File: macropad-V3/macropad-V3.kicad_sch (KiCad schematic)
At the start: 12 parts, among them SW1 SW_Push, U1 ARDUINO_PRO_MICRO

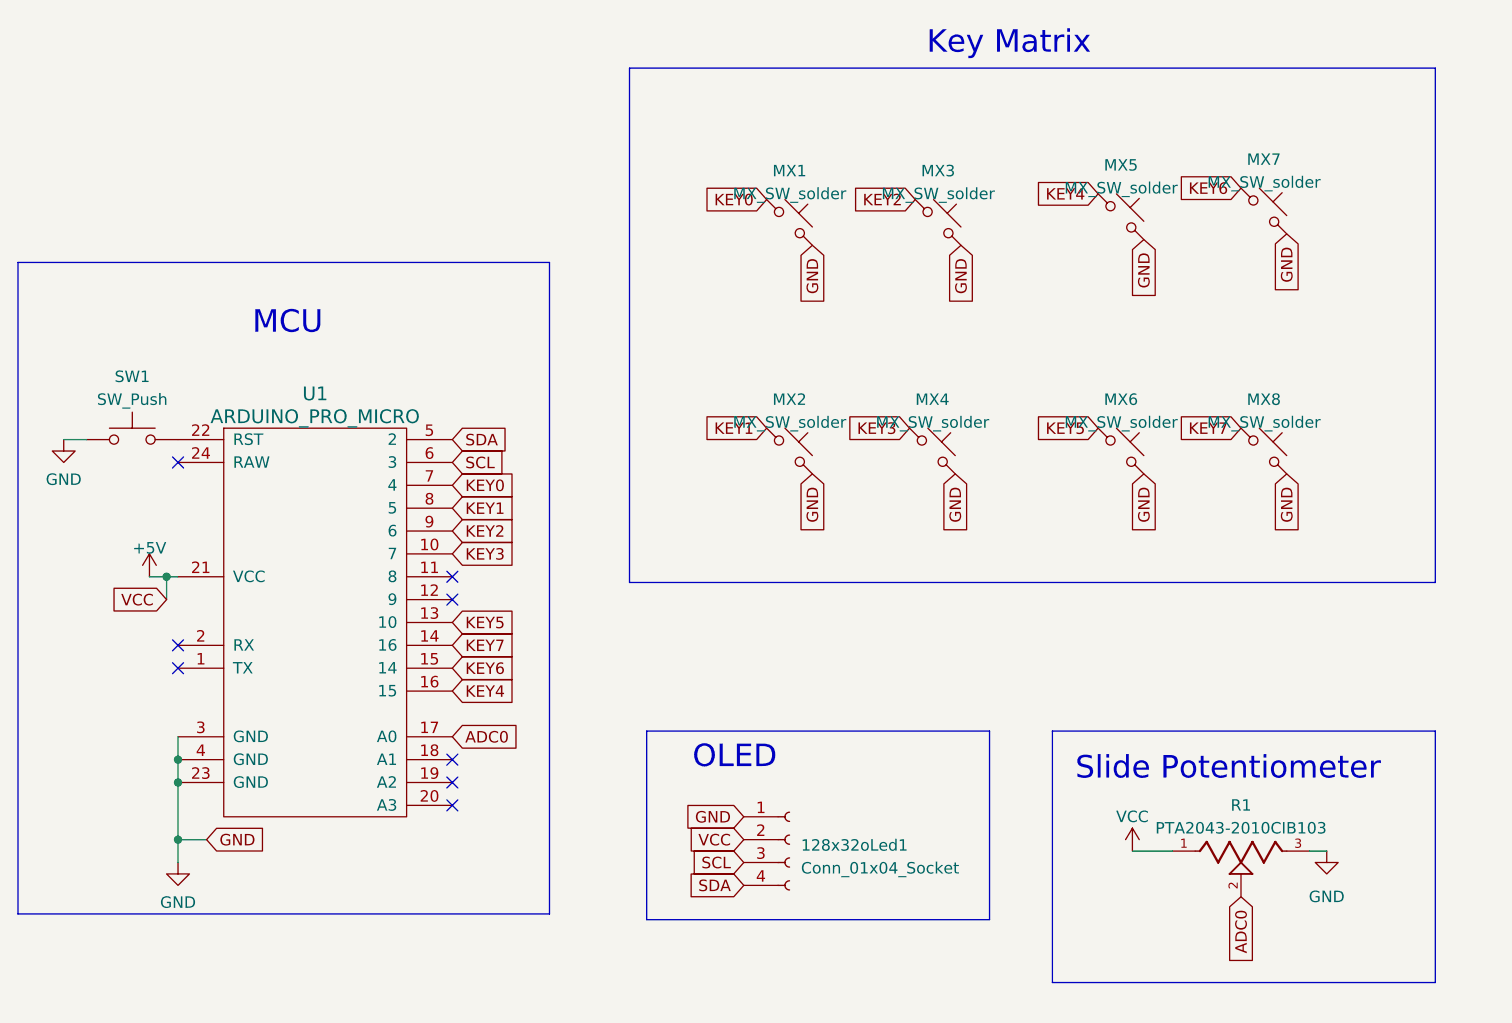
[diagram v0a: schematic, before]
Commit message: finalized schematic
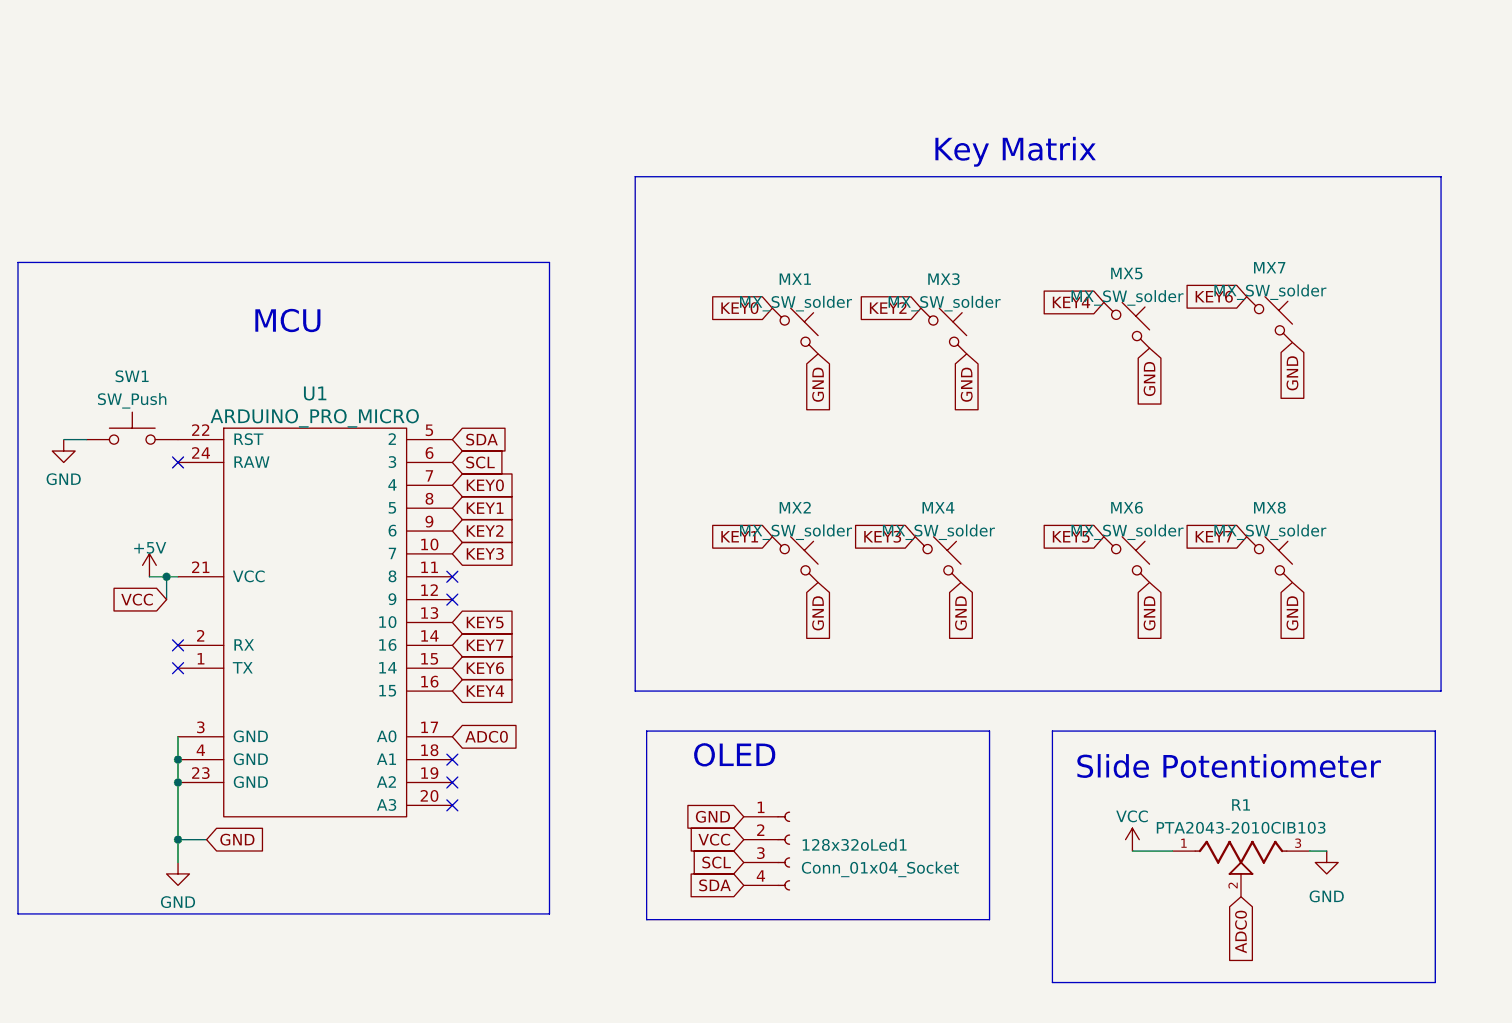
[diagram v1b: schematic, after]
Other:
- moved on the sheet: MX1, MX2, MX3, MX4, MX5, MX6, MX7, MX8

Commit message: added pull up resistors/added ground plane/routed traces
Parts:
- added R2, R3: 4.7k, Resistor_THT:R_Axial_DIN0309_L9.0mm_D3.2mm_P12.70mm_Horizontal, symbol Device:R_Small
- 128x32oLed1: symbol Connector:Conn_01x04_Socket -> Connector_Generic:Conn_01x04
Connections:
- net +5V: now also R2.2, R3.2
- net SCL: now also R2.1
- net SDA: now also R3.1
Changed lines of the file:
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@@
   (junction (at 116.84 128.27) (diameter 0) (color 0 0 0 0)
+  )
+  (junction (at 179.705 139.7) (diameter 0) (color 0 0 0 0)
+  )
+  (junction (at 178.435 137.16) (diameter 0) (color 0 0 0 0)
   )
   (junction (at 116.84 125.73) (diameter 0) (color 0 0 0 0)
@@
     (stroke (width 0) (type default))
   )
+  (wire (pts (xy 178.435 137.16) (xy 178.435 144.78))
+    (stroke (width 0) (type default))
+  )
   (wire (pts (xy 242.57 135.89) (xy 244.475 135.89))
     (stroke (width 0) (type default))
@@
     (stroke (width 0) (type default))
   )
+  (wire (pts (xy 189.23 149.86) (xy 192.405 149.86))
+    (stroke (width 0) (type default))
+  )
+  (wire (pts (xy 174.625 149.86) (xy 178.435 149.86))
+    (stroke (width 0) (type default))
+  )
   (wire (pts (xy 116.84 125.73) (xy 116.84 128.27))
     (stroke (width 0) (type default))
@@
     (stroke (width 0) (type default))
   )
+  (wire (pts (xy 179.705 144.78) (xy 192.405 144.78))
+    (stroke (width 0) (type default))
+  )
+  (wire (pts (xy 179.705 144.78) (xy 179.705 139.7))
+    (stroke (width 0) (type default))
+  )
   (wire (pts (xy 104.14 90.17) (xy 106.68 90.17))
     (stroke (width 0) (type default))
@@
     (stroke (width 0) (type default))
   )
+  (wire (pts (xy 177.8 137.16) (xy 178.435 137.16))
+    (stroke (width 0) (type default))
+  )
+  (wire (pts (xy 177.8 139.7) (xy 179.705 139.7))
+    (stroke (width 0) (type default))
+  )
+  (wire (pts (xy 178.435 137.16) (xy 179.705 137.16))
+    (stroke (width 0) (type default))
+  )
   (wire (pts (xy 116.84 123.19) (xy 116.84 125.73))
     (stroke (width 0) (type default))
@@
     (fill (type none))
   )
-  (rectangle (start 168.91 122.555) (end 207.01 143.51)
+  (rectangle (start 168.91 122.555) (end 207.01 153.035)
     (stroke (width 0) (type default))
     (fill (type none))
@@
     )
   )
-  (global_label "SCL" (shape input) (at 179.705 137.16 180) (fields_autoplaced)
-    (effects (font (size 1.27 1.27)) (justify right))
-    (property "Intersheetrefs" "${INTERSHEET_REFS}" (at 173.2916 137.16 0)
+  (global_label "SCL" (shape input) (at 177.8 137.16 180) (fields_autoplaced)
+    (effects (font (size 1.27 1.27)) (justify right))
+    (property "Intersheetrefs" "${INTERSHEET_REFS}" (at 171.3866 137.16 0)
       (effects (font (size 1.27 1.27)) (justify right) hide)
     )
@@
     )
   )
-  (global_label "SDA" (shape input) (at 179.705 139.7 180) (fields_autoplaced)
-    (effects (font (size 1.27 1.27)) (justify right))
-    (property "Intersheetrefs" "${INTERSHEET_REFS}" (at 173.2311 139.7 0)
+  (global_label "SDA" (shape input) (at 177.8 139.7 180) (fields_autoplaced)
+    (effects (font (size 1.27 1.27)) (justify right))
+    (property "Intersheetrefs" "${INTERSHEET_REFS}" (at 171.3261 139.7 0)
       (effects (font (size 1.27 1.27)) (justify right) hide)
     )
@@
     (property "Intersheetrefs" "${INTERSHEET_REFS}" (at 240.665 86.1513 90)
       (effects (font (size 1.27 1.27)) (justify right) hide)
+    )
+  )
+  (symbol (lib_id "Device:R_Small") (at 178.435 147.32 0) (unit 1)
+    (in_bom yes) (on_board yes) (dnp no) (fields_autoplaced)
+    (property "Reference" "R2" (at 180.34 146.685 0)
+      (effects (font (size 1.27 1.27)) (justify left))
+    )
+    (property "Value" "4.7k" (at 180.34 149.225 0)
+      (effects (font (size 1.27 1.27)) (justify left))
+    )
+    (property "Footprint" "Resistor_THT:R_Axial_DIN0309_L9.0mm_D3.2mm_P12.70mm_Horizontal" (at 178.435 147.32 0)
+      (effects (font (size 1.27 1.27)) hide)
+    )
+    (property "Datasheet" "~" (at 178.435 147.32 0)
+      (effects (font (size 1.27 1.27)) hide)
+    )
+    (pin "1")
+    (pin "2")
+    (instances
+      (project "macropad-V3"
+        (path "/3494e7c5-eb5a-429a-a270-84b7b5a31c13"
+          (reference "R2") (unit 1)
+        )
+      )
+    )
+  )
+  (symbol (lib_id "power:VCC") (at 132.715 132.08 0) (unit 1)
+    (in_bom yes) (on_board yes) (dnp no) (fields_autoplaced)
+    (property "Reference" "#PWR06" (at 132.715 135.89 0)
+      (effects (font (size 1.27 1.27)) hide)
+    )
+    (property "Value" "VCC" (at 132.715 128.27 0)
+      (effects (font (size 1.27 1.27)))
+    )
+    (property "Footprint" "" (at 132.715 132.08 0)
+      (effects (font (size 1.27 1.27)) hide)
+    )
+    (property "Datasheet" "" (at 132.715 132.08 0)
+      (effects (font (size 1.27 1.27)) hide)
+    )
+    (pin "1")
+    (instances
+      (project "macropad-V3"
+        (path "/3494e7c5-eb5a-429a-a270-84b7b5a31c13"
+          (reference "#PWR06") (unit 1)
+        )
+      )
     )
   )
@@
     )
   )
+  (symbol (lib_id "Device:R_Small") (at 192.405 147.32 0) (unit 1)
+    (in_bom yes) (on_board yes) (dnp no) (fields_autoplaced)
+    (property "Reference" "R3" (at 194.31 146.685 0)
+      (effects (font (size 1.27 1.27)) (justify left))
+    )
+    (property "Value" "4.7k" (at 194.31 149.225 0)
+      (effects (font (size 1.27 1.27)) (justify left))
+    )
+    (property "Footprint" "Resistor_THT:R_Axial_DIN0309_L9.0mm_D3.2mm_P12.70mm_Horizontal" (at 192.405 147.32 0)
+      (effects (font (size 1.27 1.27)) hide)
+    )
+    (property "Datasheet" "~" (at 192.405 147.32 0)
+      (effects (font (size 1.27 1.27)) hide)
+    )
+    (pin "1")
+    (pin "2")
+    (instances
+      (project "macropad-V3"
+        (path "/3494e7c5-eb5a-429a-a270-84b7b5a31c13"
+          (reference "R3") (unit 1)
+        )
+      )
+    )
+  )
   (symbol (lib_id "marbastlib-mx:MX_SW_solder") (at 201.295 103.505 0) (unit 1)
     (in_bom yes) (on_board yes) (dnp no) (fields_autoplaced)
@@
     )
   )
-  (symbol (lib_id "Connector:Conn_01x04_Socket") (at 184.785 134.62 0) (unit 1)
+  (symbol (lib_id "Connector_Generic:Conn_01x04") (at 184.785 134.62 0) (unit 1)
     (in_bom yes) (on_board yes) (dnp no) (fields_autoplaced)
     (property "Reference" "128x32oLed1" (at 186.055 135.255 0)
@@
     )
   )
+  (symbol (lib_id "power:VCC") (at 189.23 149.86 0) (unit 1)
+    (in_bom yes) (on_board yes) (dnp no) (fields_autoplaced)
+    (property "Reference" "#PWR08" (at 189.23 153.67 0)
+      (effects (font (size 1.27 1.27)) hide)
+    )
+    (property "Value" "VCC" (at 189.23 146.05 0)
+      (effects (font (size 1.27 1.27)))
+    )
+    (property "Footprint" "" (at 189.23 149.86 0)
+      (effects (font (size 1.27 1.27)) hide)
+    )
+    (property "Datasheet" "" (at 189.23 149.86 0)
+      (effects (font (size 1.27 1.27)) hide)
+    )
+    (pin "1")
+    (instances
+      (project "macropad-V3"
+        (path "/3494e7c5-eb5a-429a-a270-84b7b5a31c13"
+          (reference "#PWR08") (unit 1)
+        )
+      )
+    )
+  )
   (symbol (lib_id "marbastlib-mx:MX_SW_solder") (at 238.125 103.505 0) (unit 1)
     (in_bom yes) (on_board yes) (dnp no) (fields_autoplaced)
@@
         )
       )
+    )
+  )
+  (symbol (lib_id "power:VCC") (at 174.625 149.86 0) (unit 1)
+    (in_bom yes) (on_board yes) (dnp no) (fields_autoplaced)
+    (property "Reference" "#PWR07" (at 174.625 153.67 0)
+      (effects (font (size 1.27 1.27)) hide)
+    )
+    (property "Value" "VCC" (at 174.625 146.05 0)
+      (effects (font (size 1.27 1.27)))
+    )
+    (property "Footprint" "" (at 174.625 149.86 0)
+      (effects (font (size 1.27 1.27)) hide)
+    )
+    (property "Datasheet" "" (at 174.625 149.86 0)
+      (effects (font (size 1.27 1.27)) hide)
+    )
+    (pin "1")
+    (instances
+      (project "macropad-V3"
+        (path "/3494e7c5-eb5a-429a-a270-84b7b5a31c13"
+          (reference "#PWR07") (unit 1)
+        )
+      )
